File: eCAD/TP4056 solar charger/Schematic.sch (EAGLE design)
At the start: 18 parts, among them IC1 TP4056X, IC2 AP9101CK6-ADTRG1, IC3 FDS6898A

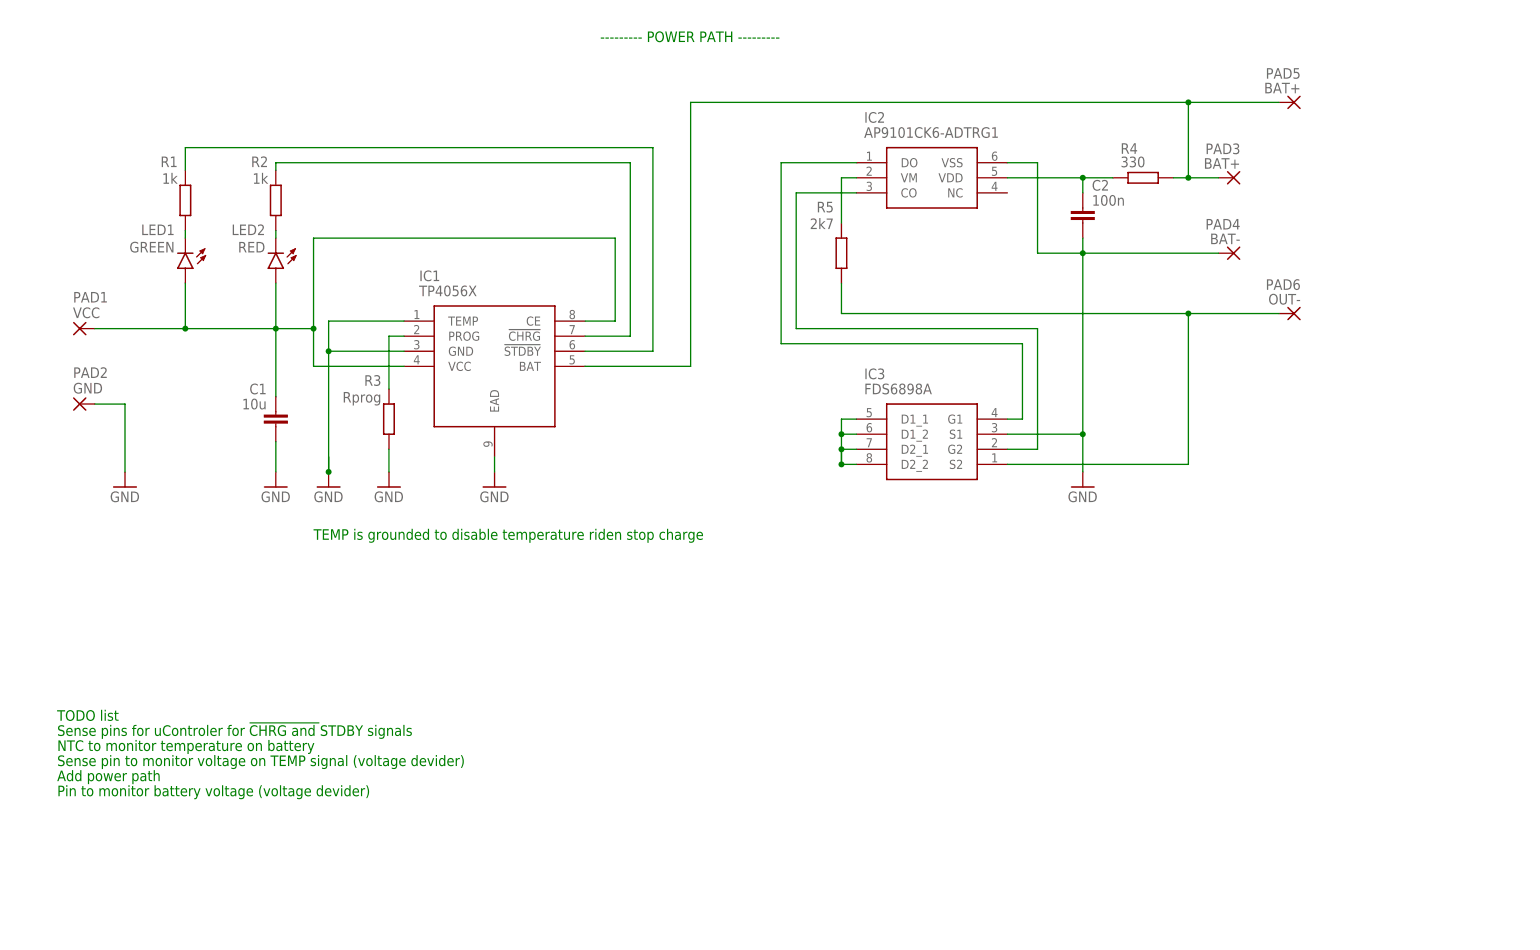
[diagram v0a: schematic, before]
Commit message: Changed packeges to 0805
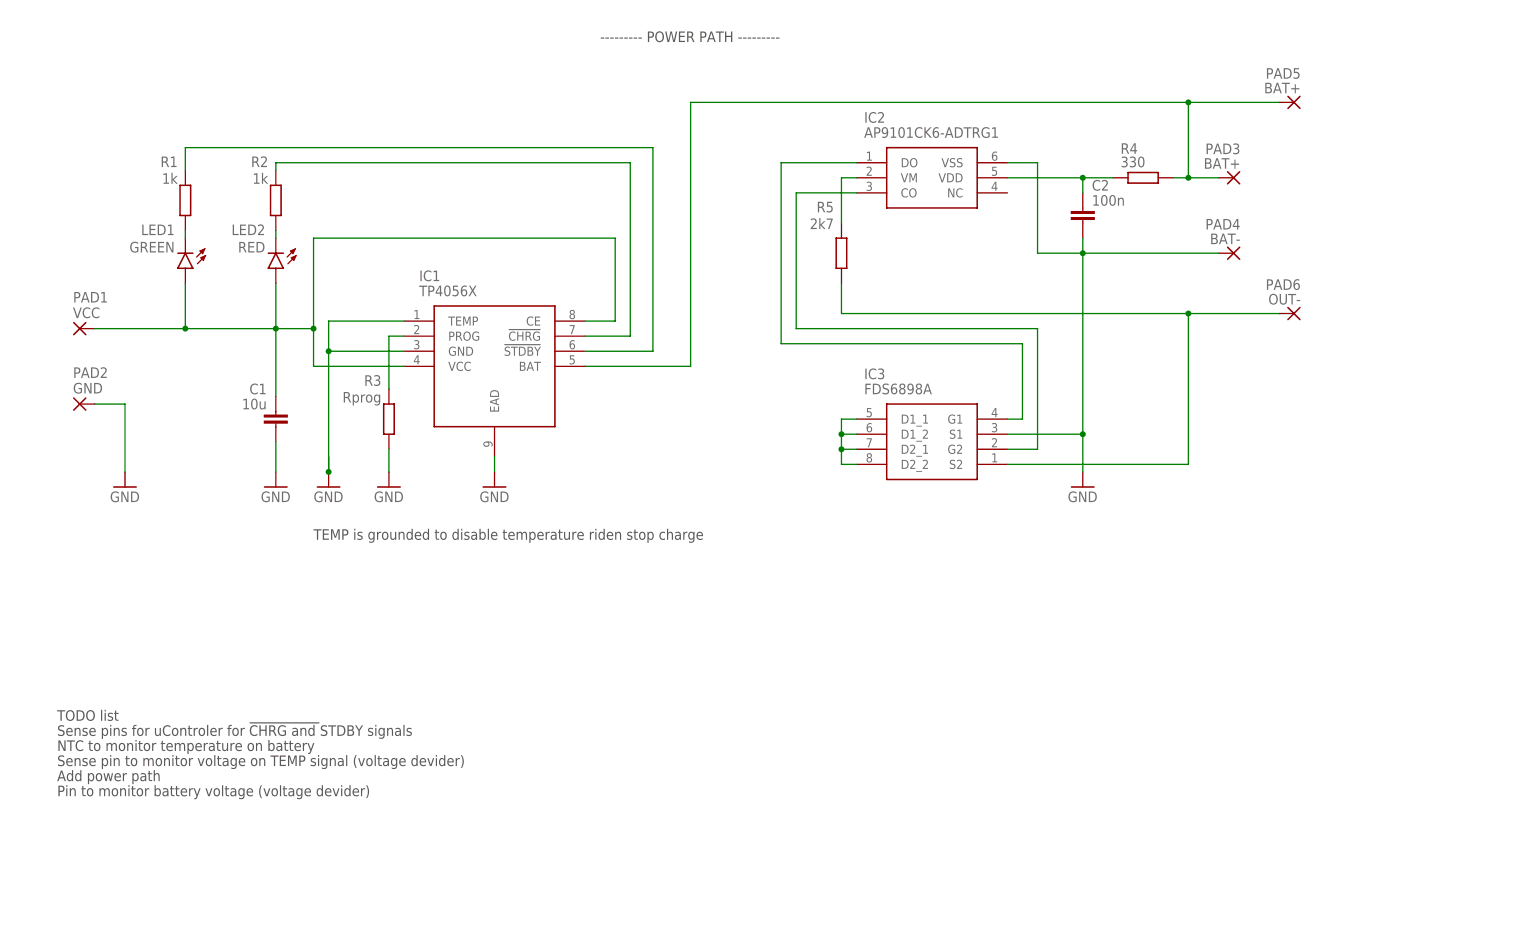
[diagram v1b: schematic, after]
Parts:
- C1, C2: device rcl:C-EUC1206 -> rcl:C-EUC0805
- LED1, LED2: device led:LEDCHIPLED_1206 -> led:LEDCHIPLED_0805
- R1, R2, R3, R4, R5: device rcl:R-EU_R1206 -> rcl:R-EU_R0805

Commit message: Schematic export to pdf and png
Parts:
- removed PAD5: BAT+, wirepad:1,6/0,8
- removed PAD6: OUT-, wirepad:1,6/0,8
- added D1: STPS2L30A, 1-component-search:STPS2L30A
- added Q1: SI2347DS-T1-GE3, 1-component-search:SI2347DS-T1-GE3
- added R6: 10k, rcl:R-EU_R0805
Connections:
- removed net N$11: IC3.S2, PAD6.P, R5.1
- removed net N$3 (its old number): C1.1, IC1.CE, IC1.VCC, LED1.A, LED2.A, PAD1.P
- removed net N$8: IC1.BAT, PAD3.P, PAD5.P, R4.2
- new net OUPUT: IC1.BAT
- new net OUT+: D1.K, Q1.S
- new net OUT-: IC3.S2, R5.1
- new net OUTPUT: PAD3.P, Q1.D, R4.2
- new net POWER_PATH: C1.1, D1.A, IC1.CE, IC1.VCC, LED1.A, LED2.A, PAD1.P, Q1.G, R6.2
- net GND: now also R6.1
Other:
- note added: "LDO regulator on output"
- note added: "✔"
- note removed: "--------- POWER PATH ---------"
- moved on the sheet: C1, C2, IC1, IC2, IC3, LED1, LED2, PAD1, PAD2, PAD3, PAD4, R1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

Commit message: Board design
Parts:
- removed PAD1: VCC, wirepad:1,6/0,8
- removed PAD2: GND, wirepad:1,6/0,8
- removed PAD3: BAT+, wirepad:1,6/0,8
- removed PAD4: BAT-, wirepad:1,6/0,8
- added C3, C4: 470n, rcl:C-EUC0805
- added C5: 10u, rcl:C-EUC0805
- added JP1: !CHRG, pinhead:PINHD-1X1
- added JP2: !STDBY, pinhead:PINHD-1X1
- added JP3: VIN, pinhead:PINHD-1X1
- added JP4: OUT+, pinhead:PINHD-1X1
- added JP5: BAT_V, pinhead:PINHD-1X1
- added PS1: BU33SD5WG-TR, 1-component-search:BU33SD5WG-TR
- added R10: 27K, rcl:R-EU_R0805
- added R11: 100k, rcl:R-EU_R0805
- added R7, R8: 5k1, rcl:R-EU_R0805
- added R9: 1M, rcl:R-EU_R0805
- added U$1: USBC-6P, USBC6P:USBC-6P
- added X1: PV_PANEL, con-ptr500:AK300/2
- added X2: BATTERY, con-ptr500:AK300/2
- added X3: OUTPUT, con-ptr500:AK300/2
- R4: value 330 -> 330R
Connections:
- removed net OUT-: IC3.S2, R5.1
- removed net POWER_PATH: C1.1, D1.A, IC1.CE, IC1.VCC, LED1.A, LED2.A, PAD1.P, Q1.G, R6.2
- new net BAT-: C2.2, IC2.VSS, IC3.S1, X2-2.KL
- new net N$11: R7.2, U$1.CC1
- new net N$14: C4.1, PS1.VOUT, X3-1.KL
- new net N$15: JP5.1, R10.1, R11.2
- new net N$7: R9.1, U$1.S
- new net N$8: R8.2, U$1.CC2
- new net VIN: C1.1, D1.A, IC1.CE, IC1.VCC, JP3.1, LED1.A, LED2.A, Q1.G, R6.2, U$1.VBUS, X1-1.KL
- net GND: now also C3.2, C4.2, C5.2, IC3.S2, PS1.GND, R11.1, R5.1, R7.1, R8.1, R9.2, U$1.GND, X1-2.KL, X3-2.KL; no longer C2.2, IC2.VSS, IC3.S1, PAD2.P, PAD4.P
- net N$3: now also JP2.1
- net N$6: now also JP1.1
- net OUT+: now also C3.1, JP4.1, PS1.STBY, PS1.VIN
- net OUTPUT: now also C5.1, R10.2, X2-1.KL; no longer PAD3.P
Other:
- note removed: "Add power path"
- note removed: "LDO regulator on output"
- note removed: "NTC to monitor temperature on battery"
- note removed: "Pin to monitor battery voltage (voltage devider)"
- note removed: "Sense pin to monitor voltage on TEMP signal (voltage devider)"
- note removed: "Sense pins for uControler for !CHRG and !STDBY signals"
- note removed: "TODO list"
- note removed: "✔"
- moved on the sheet: C1, C2, D1, IC1, IC2, IC3, LED1, LED2, Q1, R1, R2, R3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
